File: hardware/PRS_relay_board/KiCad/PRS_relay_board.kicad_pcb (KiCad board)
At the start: 4 copper layers, 160 x 137 mm, 115 parts, among them J1 691313410004, J2 691313410004, J3 UJ2-BH-2-TH, J4 FTSH-105-01-F-DV-K-P, J5 10-32-1031, J6 B3B-XH-A, K1 1-1393210-3, K2 1-1393210-3, K3 1-1393210-3, K4 1-1393210-3, Q1 PMV37ENEA, Q2 PMV37ENEA, Q3 PMV37ENEA, Q4 PMV37ENEA, Q5 BC848, Q6 PMV37ENEA, U1 STCN75, U2 STM32L062K8Tx, U3 74LVC125AD,118, U4 USBLC6-2SC6, U5 UA78M33CKVURG3

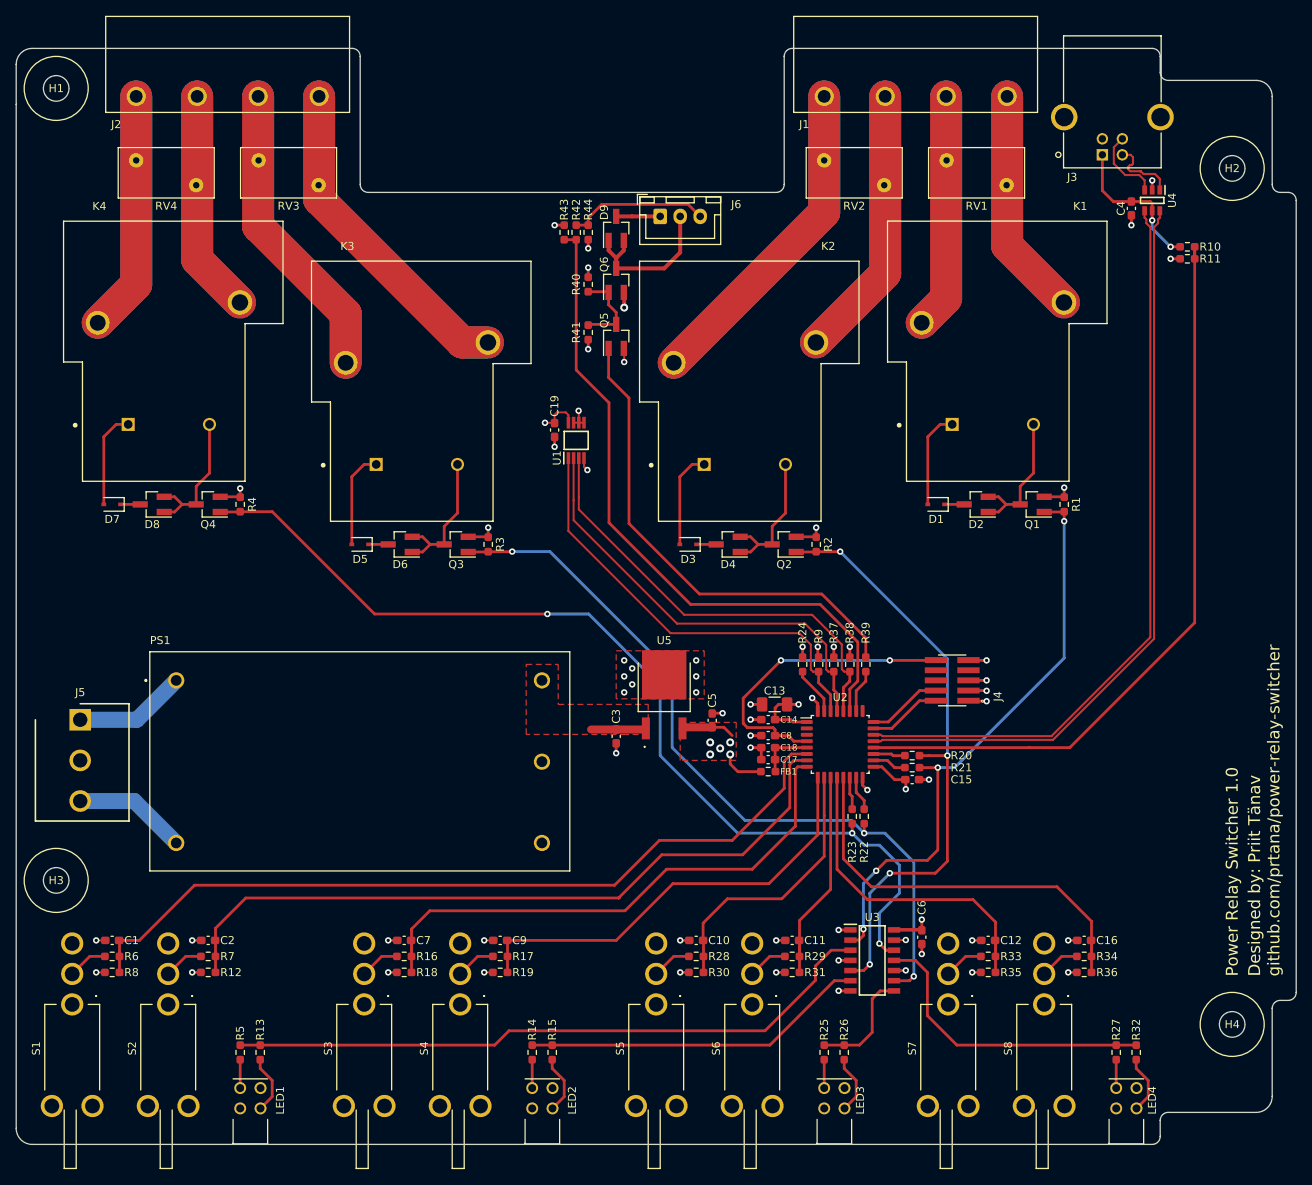
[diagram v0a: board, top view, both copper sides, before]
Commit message: Update PRS_relay_board.kicad_pcb to KiCad v6
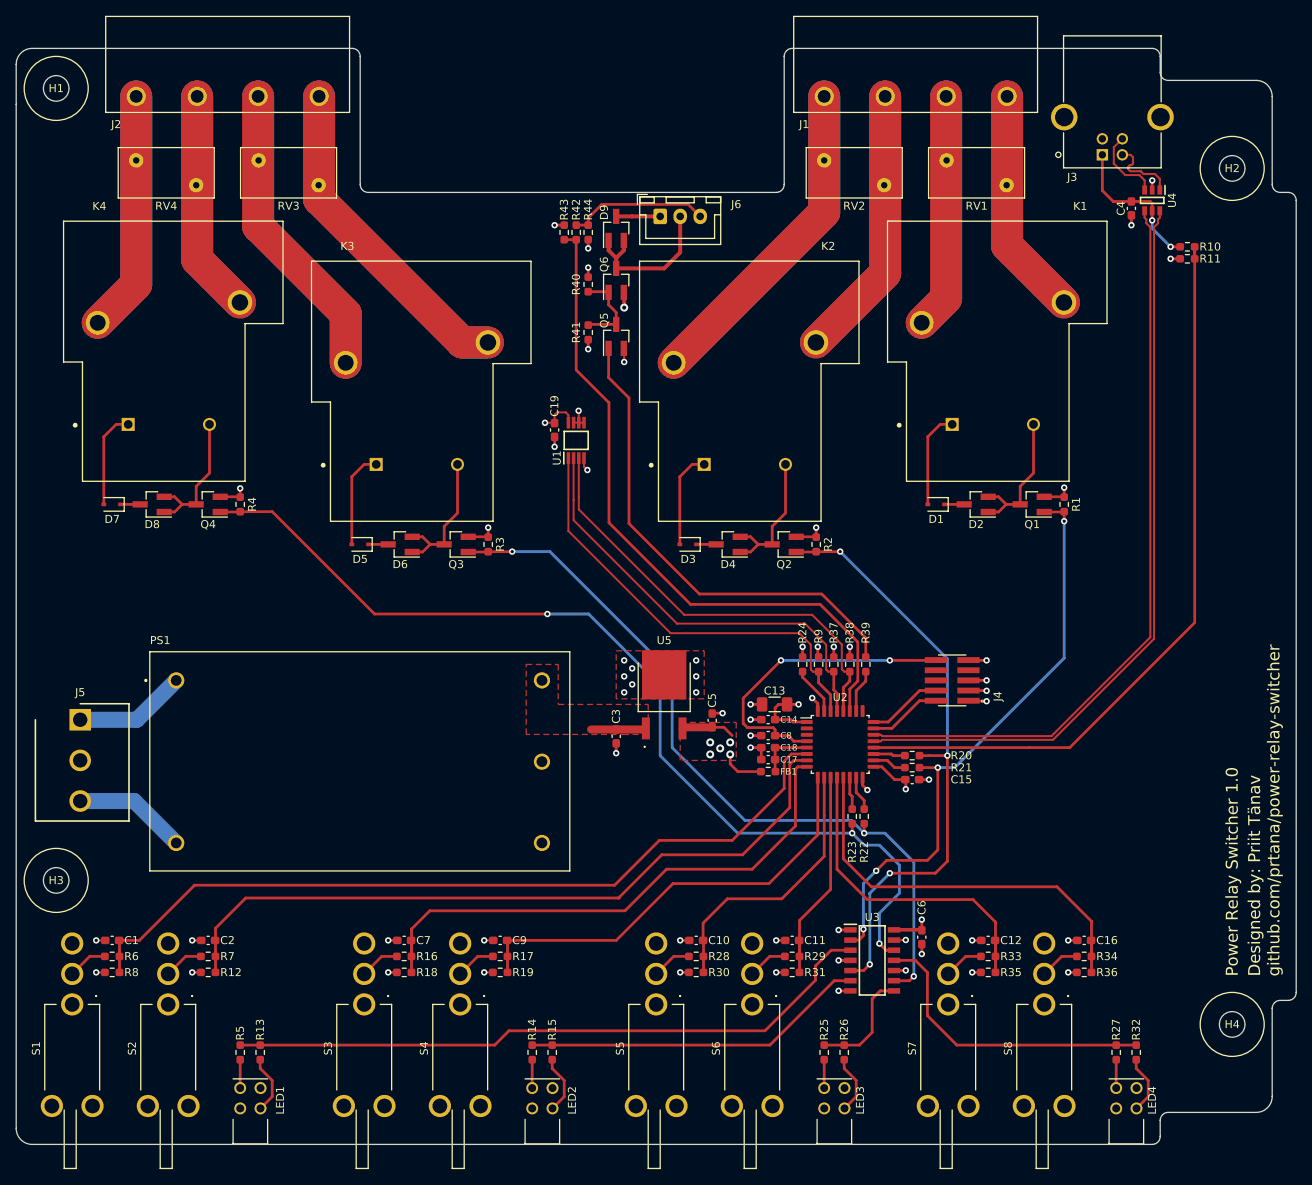
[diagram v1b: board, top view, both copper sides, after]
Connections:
- net /MCU/~RST renamed /MCU/~{RST}
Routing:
- added copper zone on In2.Cu, net +12V
- added copper zone on In2.Cu, net +3V3
- added copper zone on In1.Cu, net GND
- removed copper zone on PWR, net +12V
- removed copper zone on PWR, net +3V3
- removed copper zone on GND, net GND
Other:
- net class Default removed
- net class RELAY removed

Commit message: Fix 3d model paths
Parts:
- R40: value 1k -> 10k
- R41: value 10k -> -
- R42, R43: value R -> 4k7
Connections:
- J4 pad 6: Net-(J4-Pad6) -> unconnected-(J4-Pad6)
- J4 pad 7: Net-(J4-Pad7) -> unconnected-(J4-Pad7)
- J4 pad 8: Net-(J4-Pad8) -> unconnected-(J4-Pad8)
- J5 pad 2: Net-(J5-Pad2) -> unconnected-(J5-Pad2)
- PS1 pad 3: Net-(PS1-Pad3) -> unconnected-(PS1-Pad3)
- S1 pad 1: Net-(S1-Pad1) -> unconnected-(S1-Pad1)
- S1 pad MH1: Net-(S1-PadMH1) -> unconnected-(S1-PadMH1)
- S1 pad MH2: Net-(S1-PadMH2) -> unconnected-(S1-PadMH2)
- S2 pad 1: Net-(S2-Pad1) -> unconnected-(S2-Pad1)
- S2 pad MH1: Net-(S2-PadMH1) -> unconnected-(S2-PadMH1)
- S2 pad MH2: Net-(S2-PadMH2) -> unconnected-(S2-PadMH2)
- S3 pad 1: Net-(S3-Pad1) -> unconnected-(S3-Pad1)
- S3 pad MH1: Net-(S3-PadMH1) -> unconnected-(S3-PadMH1)
- S3 pad MH2: Net-(S3-PadMH2) -> unconnected-(S3-PadMH2)
- S4 pad 1: Net-(S4-Pad1) -> unconnected-(S4-Pad1)
- S4 pad MH1: Net-(S4-PadMH1) -> unconnected-(S4-PadMH1)
- S4 pad MH2: Net-(S4-PadMH2) -> unconnected-(S4-PadMH2)
- S5 pad 1: Net-(S5-Pad1) -> unconnected-(S5-Pad1)
- S5 pad MH1: Net-(S5-PadMH1) -> unconnected-(S5-PadMH1)
- S5 pad MH2: Net-(S5-PadMH2) -> unconnected-(S5-PadMH2)
- S6 pad 1: Net-(S6-Pad1) -> unconnected-(S6-Pad1)
- S6 pad MH1: Net-(S6-PadMH1) -> unconnected-(S6-PadMH1)
- S6 pad MH2: Net-(S6-PadMH2) -> unconnected-(S6-PadMH2)
- S7 pad 1: Net-(S7-Pad1) -> unconnected-(S7-Pad1)
- S7 pad MH1: Net-(S7-PadMH1) -> unconnected-(S7-PadMH1)
- S7 pad MH2: Net-(S7-PadMH2) -> unconnected-(S7-PadMH2)
- S8 pad 1: Net-(S8-Pad1) -> unconnected-(S8-Pad1)
- S8 pad MH1: Net-(S8-PadMH1) -> unconnected-(S8-PadMH1)
- S8 pad MH2: Net-(S8-PadMH2) -> unconnected-(S8-PadMH2)
- U2 pad 2: Net-(U2-Pad2) -> unconnected-(U2-Pad2)
- U2 pad 25: Net-(U2-Pad25) -> unconnected-(U2-Pad25)
- U2 pad 3: Net-(U2-Pad3) -> unconnected-(U2-Pad3)
